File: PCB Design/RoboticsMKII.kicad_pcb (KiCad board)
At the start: 4 copper layers, 92 parts, among them CON1 USB, CON2 BARREL_JACK, P1 Power Sel, P10 CONN_02X12, P11 DAC, P12 Reed, P13 SPI, P14 ICSP, P15 Gnd, P16 UART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

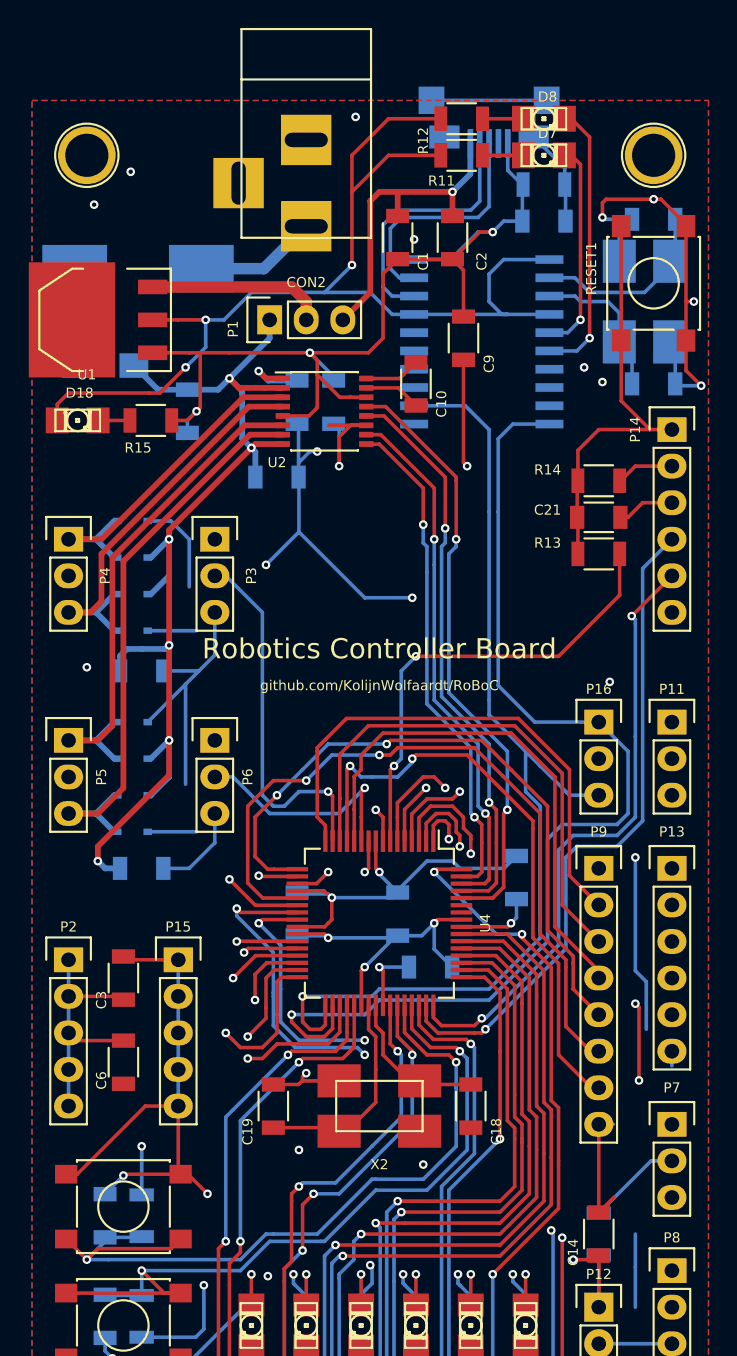
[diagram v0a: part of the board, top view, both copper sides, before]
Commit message: More Changes:
Checked top and bottom silkscreen - almost no overlaps with pads or holes
Added Robotic club logo to board, generated from png file.
Modified on-board text.

Signed-off-by: Kolijn Wolfaardt <kolijn.wolfaardt@gmail.com>
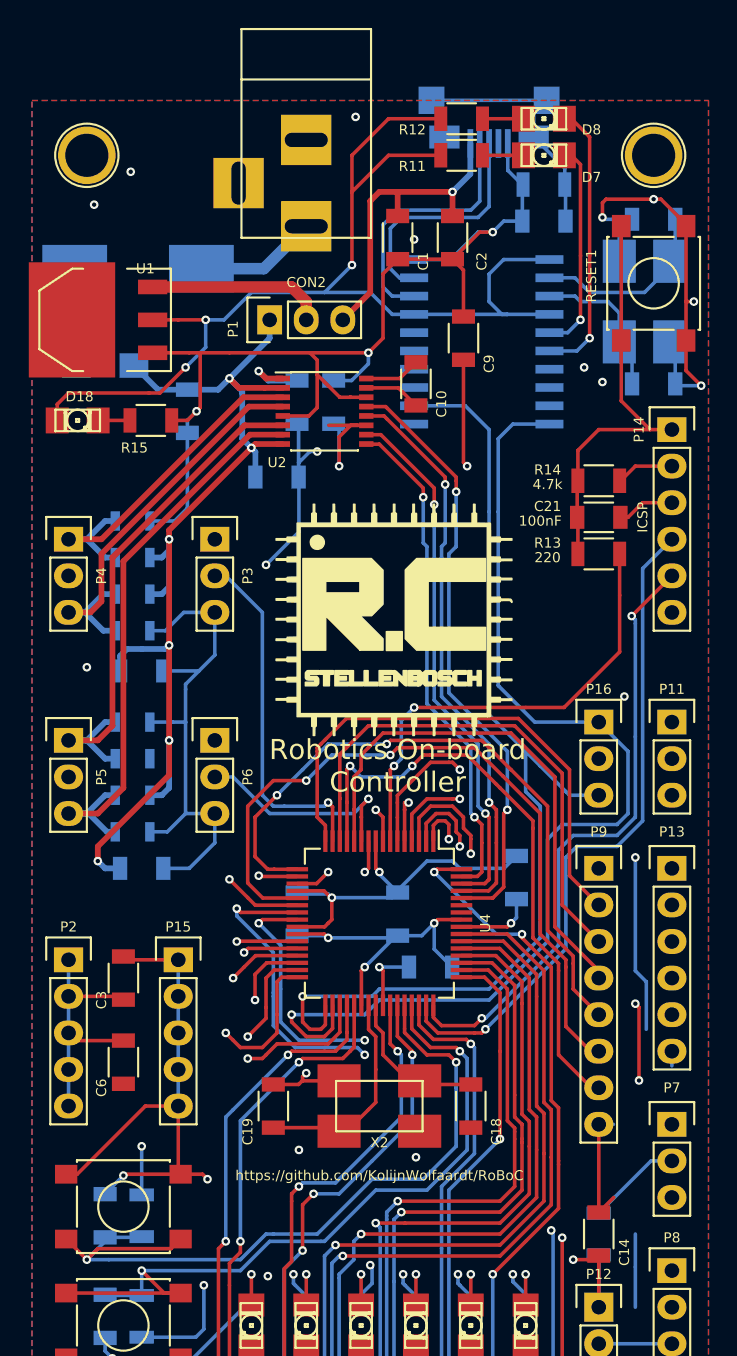
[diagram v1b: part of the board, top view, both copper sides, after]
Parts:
- added G***: LOGO, RoBoC:RoBoC_Logo, F.Cu at (138.2, 79.2)
- D10, D11, D12, D13, D14, D15, D16, D17: footprint Diodes_SMD:SOD-323 -> RoBoC:SOD-323
- P10: value CONN_02X12 -> Camera
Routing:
- net /gpio/DACOUT: track 42.4 -> 31.9 mm
- net GND: track 475.0 -> 481.1 mm, vias 26 -> 25
- net /gpio/SPI_MOSI: track 29.4 -> 32.8 mm
- net /motors/V_Bat: track 79.5 -> 77.6 mm
- net /motors/MOT2_2: track 40.9 -> 42.5 mm
- net /motors/MOT2_1: track 36.7 -> 38.3 mm
- net /mcu/MOT1_ENC: track 25.9 -> 24.9 mm
- net /gpio/SPI_MISO: track 30.6 -> 29.7 mm
- net /mcu/MOT2_ENC: track 16.0 -> 15.3 mm
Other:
- board text added: "Robotics On-board Controller"
- board text added: "https://github.com/KolijnWolfaardt/RoBoC"
- board text removed: "Robotics Controller Board"
- board text removed: "github.com/KolijnWolfaardt/RoBoC"

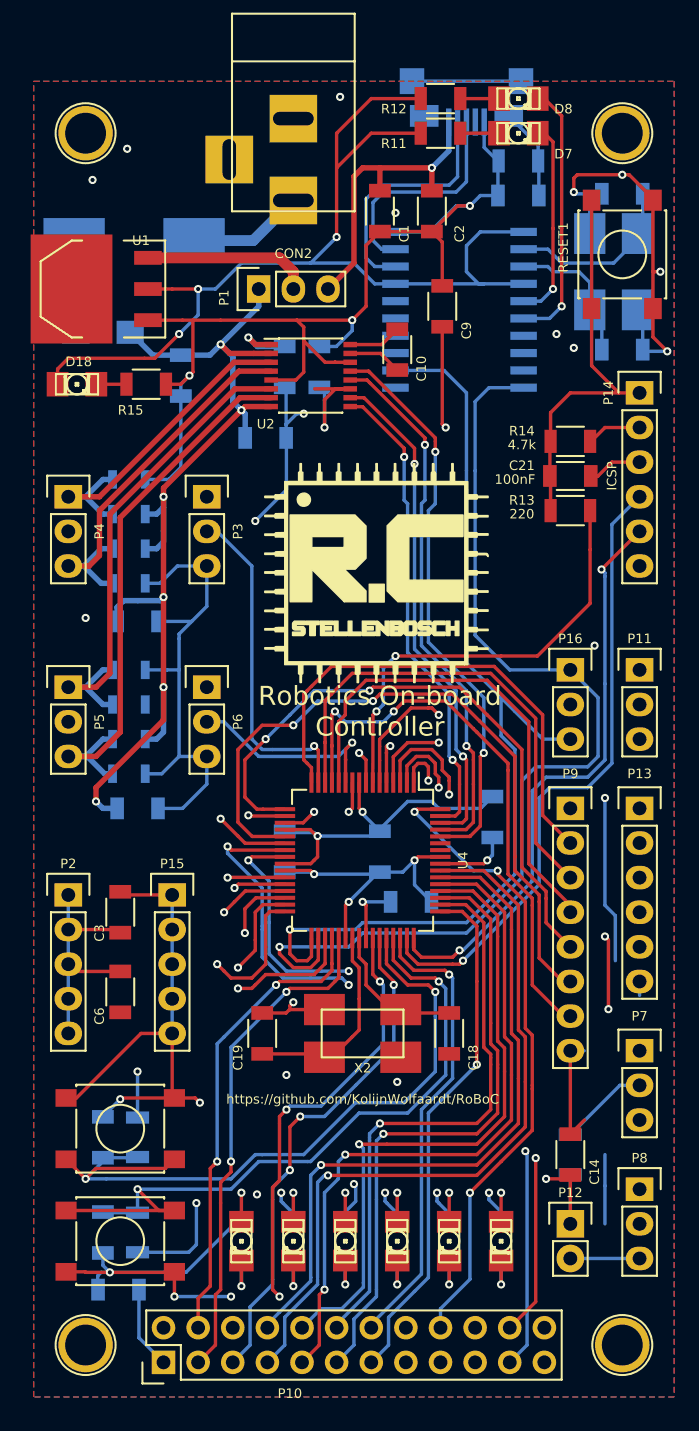
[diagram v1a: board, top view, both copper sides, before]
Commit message: Moved all fabrication layer to silkscreen
Moved tracks to look better with copper pour
Fixed more silscreen-on-via errors

Signed-off-by: Kolijn Wolfaardt <kolijn.wolfaardt@gmail.com>
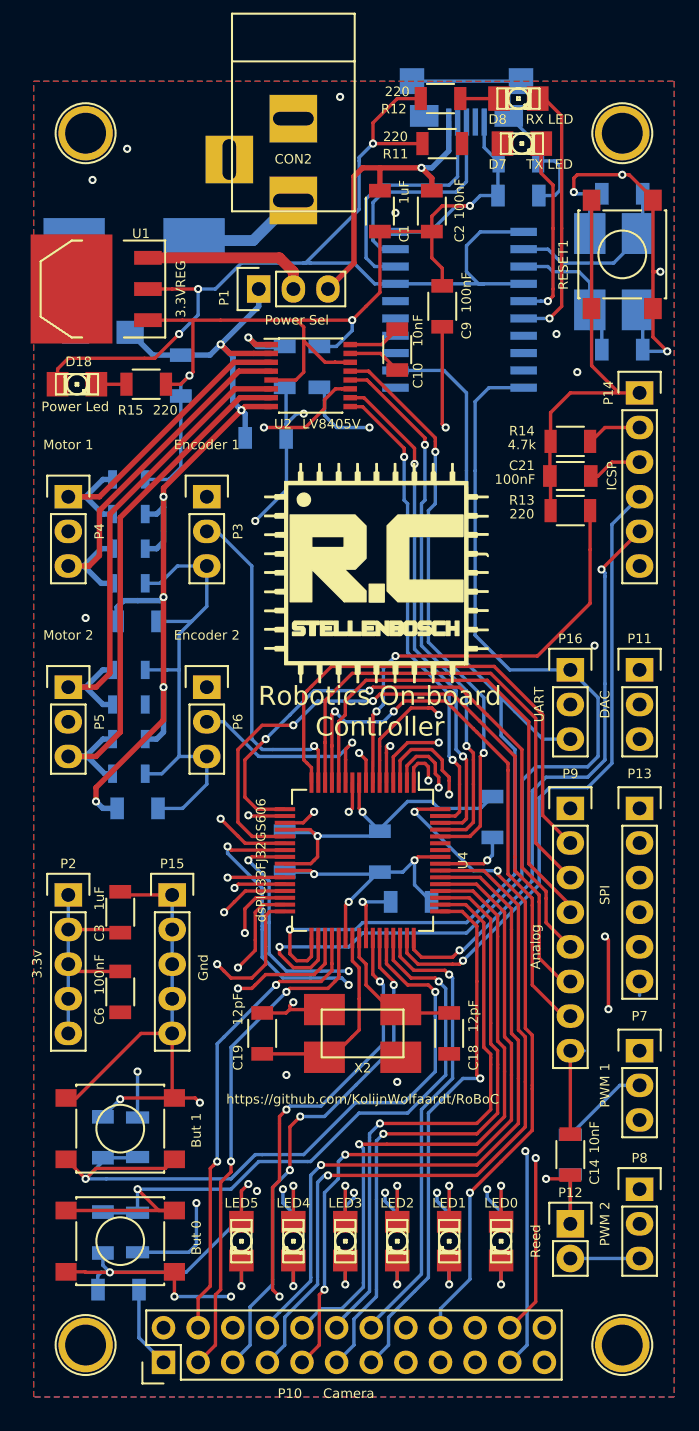
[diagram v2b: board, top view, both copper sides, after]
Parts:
- moved D7 0.80 mm to (148.8, 47.8)
- moved R11 0.77 mm to (143.0, 47.8)
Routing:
- net (no net): track 24.2 -> 5.08 mm, vias 10 -> 9
- net Net-(D7-Pad1): track 2.85 -> 0.00 mm
- net Net-(C17-Pad1): track 20.6 -> 23.4 mm
- net GND: track 481.1 -> 479.8 mm
- net /gpio/DATA_1: track 38.9 -> 39.9 mm
- net /usb/TX_LED: track 14.7 -> 13.9 mm
- net V3.3: vias 12 -> 13

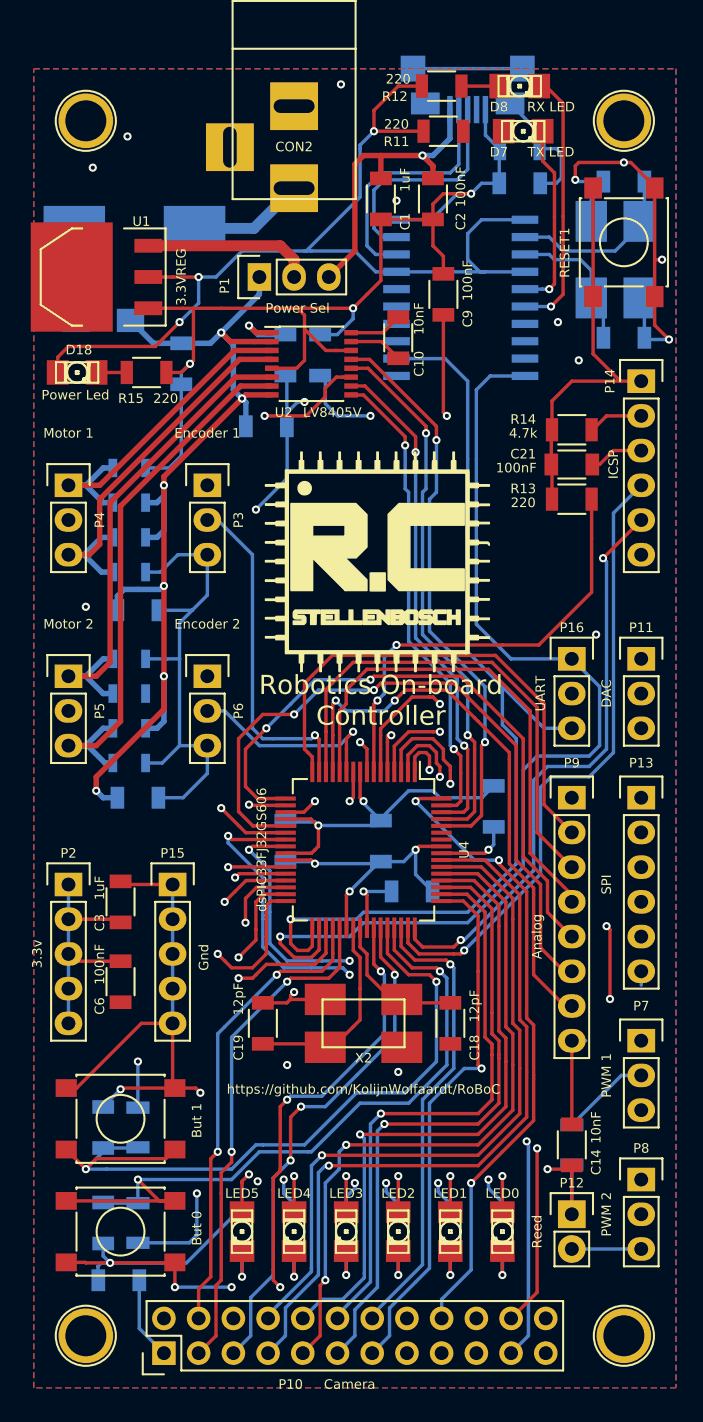
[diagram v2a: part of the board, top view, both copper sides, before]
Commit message: Added keepout under some components
Signed-off-by: Kolijn Wolfaardt <kolijn.wolfaardt@gmail.com>
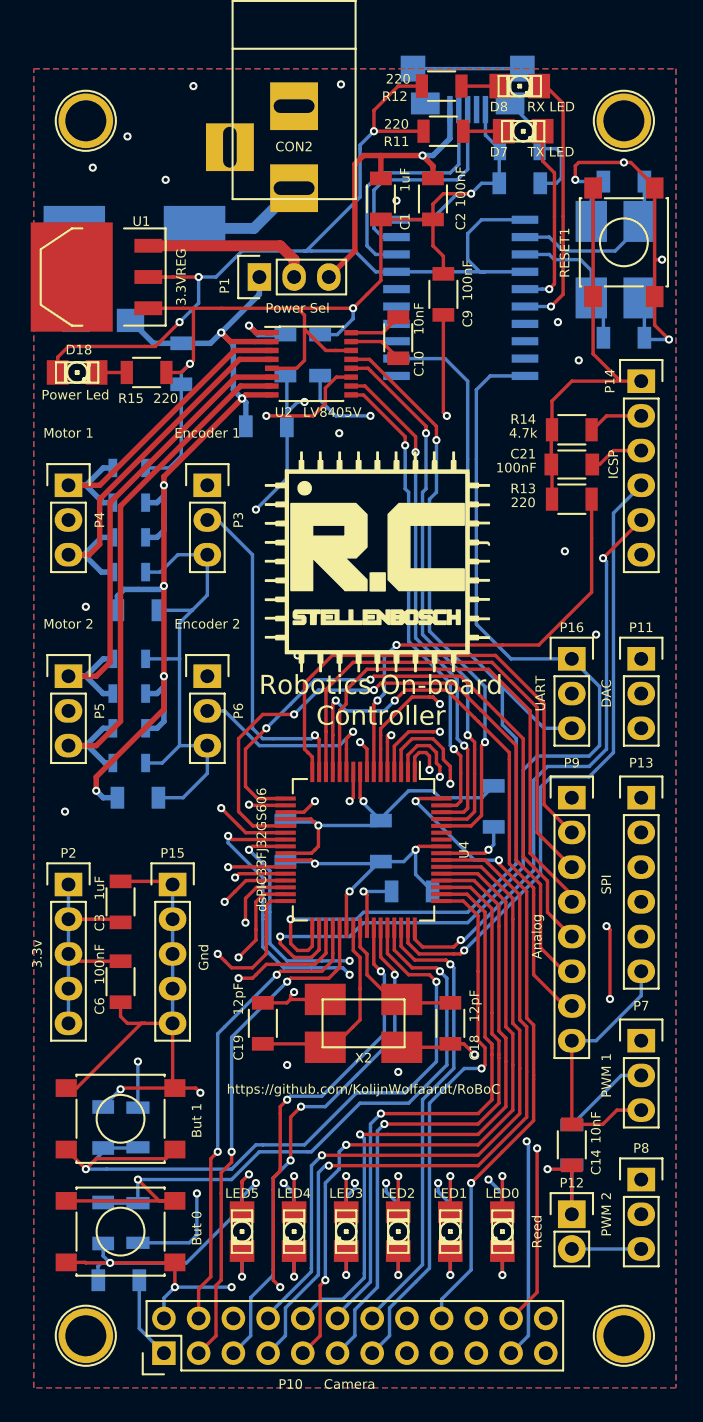
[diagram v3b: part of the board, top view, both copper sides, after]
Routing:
- net GND: track 479.8 -> 577.9 mm, vias 25 -> 26
- net /gpio/DACOUT: track 31.9 -> 43.4 mm
- net Net-(D7-Pad1): track 0.00 -> 2.97 mm
- net /motors/V_Bat: track 77.6 -> 79.2 mm
- net V3.3: track 482.3 -> 483.1 mm
- net (no net): vias 9 -> 15

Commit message: Some small changes
Signed-off-by: Kolijn Wolfaardt <kolijn.wolfaardt@gmail.com>
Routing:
- net V3.3: track 483.1 -> 484.3 mm
- net GND: track 577.9 -> 579.1 mm

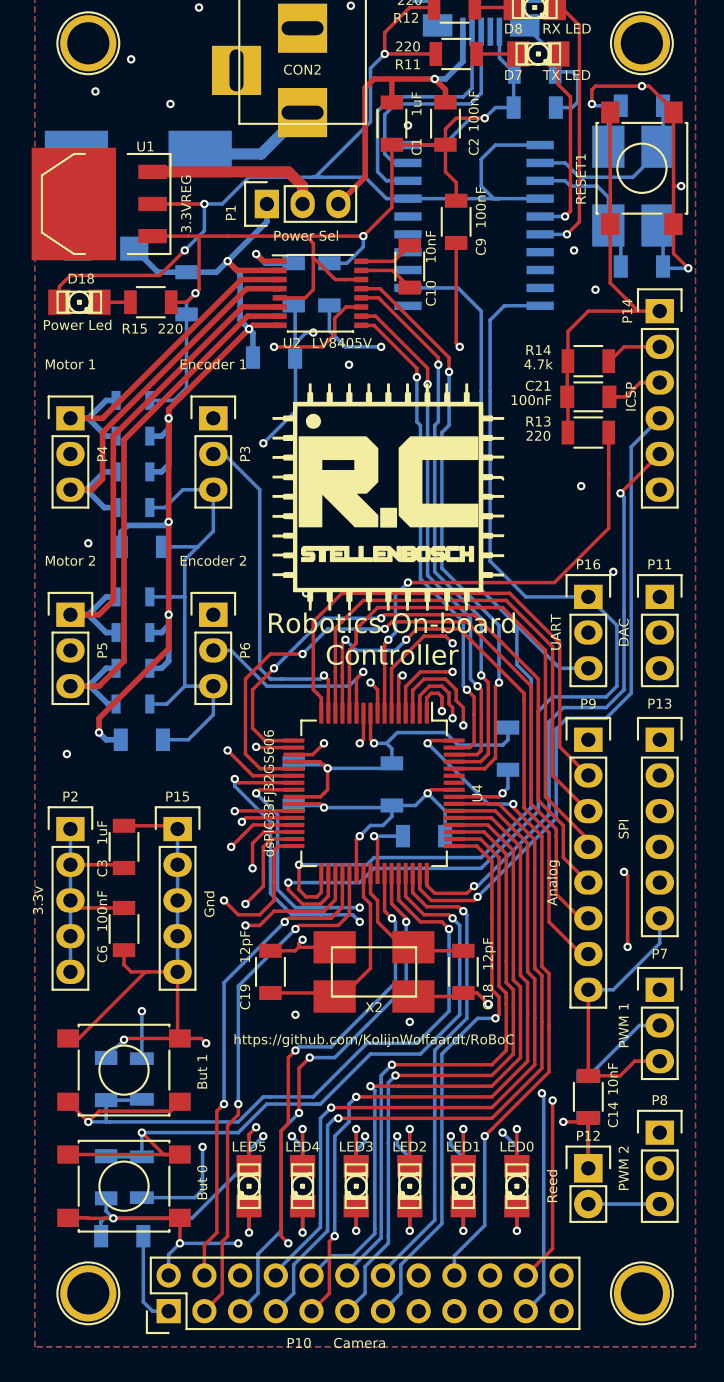
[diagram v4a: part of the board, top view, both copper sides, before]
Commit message: Increased pad sizes for easy soldering, final commit before ordering
Signed-off-by: Kolijn Wolfaardt <kolijn.wolfaardt@gmail.com>
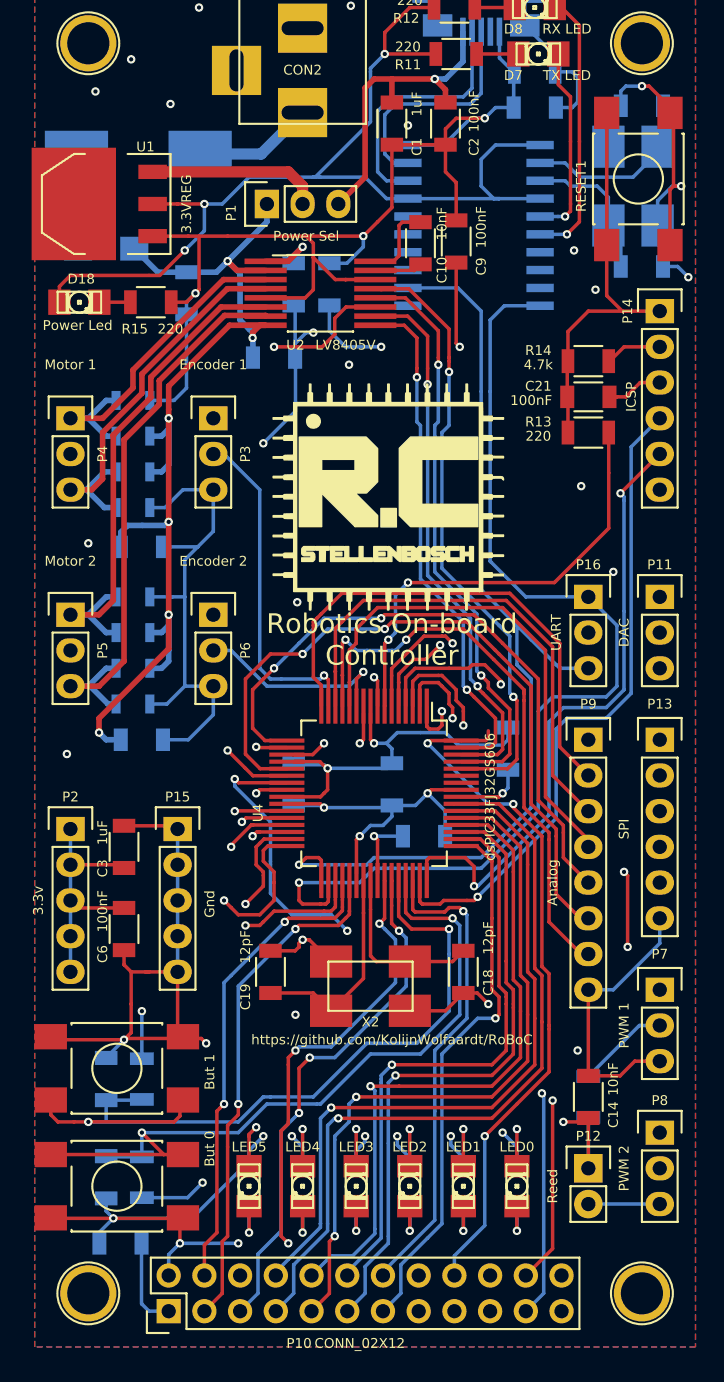
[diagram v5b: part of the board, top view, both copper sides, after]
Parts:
- P10: value Camera -> CONN_02X12
- RESET1, SW0, SW1: footprint Buttons_Switches_SMD:SW_SPST_PTS645 -> RoBoC:SW_SPST_bigpads
- U2: footprint Housings_SSOP:SSOP-16_4.4x5.2mm_Pitch0.65mm -> RoBoC:SSOP-16_4.4x5.2mm_Pitch0.65mm_Handsoldering
- U4: footprint Housings_QFP:TQFP-64_10x10mm_Pitch0.5mm -> RoBoC:TQFP-64_10x10mm_Pitch0.5mm_handsoldering
- moved C10 1.82 mm to (140.5, 61.2)
- moved C9 1.40 mm to (143.0, 61.1)
- moved X2 1.05 mm to (136.9, 114.0)
- moved RESET1 0.80 mm to (156.0, 56.6)
- moved C5 0.52 mm to (119.1, 132.3)
- moved SW1 0.52 mm to (118.9, 119.9)
- moved SW0 0.51 mm to (118.9, 128.3)
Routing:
- net GND: track 579.1 -> 589.0 mm, vias 26 -> 25
- net V3.3: track 484.3 -> 479.8 mm
- net /gpio/SPI_MISO: track 29.7 -> 33.4 mm
- net /mcu/OSC1: track 10.6 -> 13.9 mm
- net /gpio/RCK: track 47.2 -> 50.2 mm
- net /mcu/MOT2_D1: track 37.1 -> 39.0 mm
- net /mcu/MOT2_D2: track 35.5 -> 37.4 mm
- net /mcu/PGC: track 43.0 -> 44.9 mm
- net /mcu/MOT1_D2: track 39.8 -> 41.5 mm
- net /mcu/MOT1_D1: track 42.0 -> 43.8 mm
- net /motors/C1H: track 3.92 -> 5.63 mm
- net /mcu/MOT2_ENC: track 15.3 -> 13.6 mm
- net /gpio/SPI_MOSI: track 32.8 -> 31.1 mm
- net /gpio/AN3: track 46.4 -> 44.8 mm
- net /gpio/BUT_1: track 54.6 -> 56.1 mm
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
